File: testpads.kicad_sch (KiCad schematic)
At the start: 7 parts, among them J12 PinHeader_2x5_P1.27mm_SMD, J13 PinHeader_2x5_P1.27mm_SMD, J14 PinHeader_2x5_P1.27mm_SMD, J15 PinHeader_2x5_P1.27mm_SMD, J16 PinHeader_2x5_P1.27mm_SMD, J17 PinHeader_2x5_P1.27mm_SMD, J20 PinHeader_2x5_P1.27mm_SMD

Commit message: [#93514] Propagate title and date across all of the sheets
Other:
- title: (none) -> Datacenter Secure Control Module Breakout Board
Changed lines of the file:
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@@
 	(generator_version "9.0")
 	(paper "A3")
+	(title_block
+		(title "Datacenter Secure Control Module Breakout Board")
+		(date "2021-12-16")
+		(rev "2.0.0")
+	)
 	(text "I2C"
 		(exclude_from_sim no)

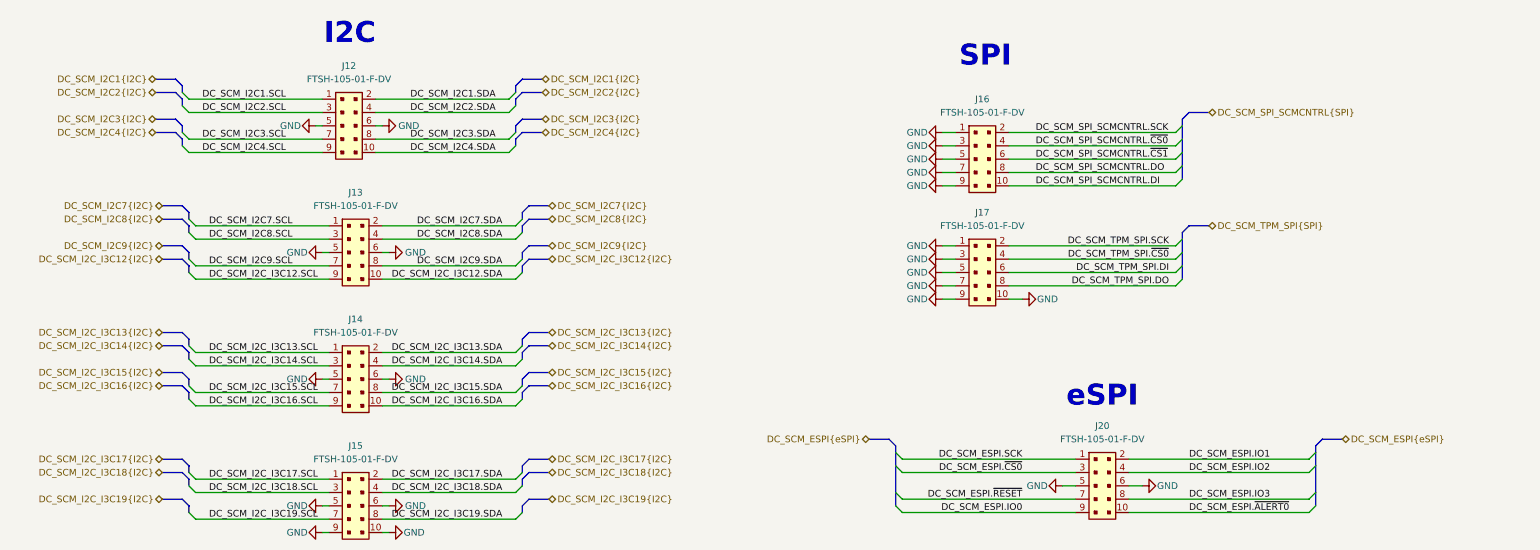
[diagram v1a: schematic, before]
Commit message: [#93514] Move SPI to one header
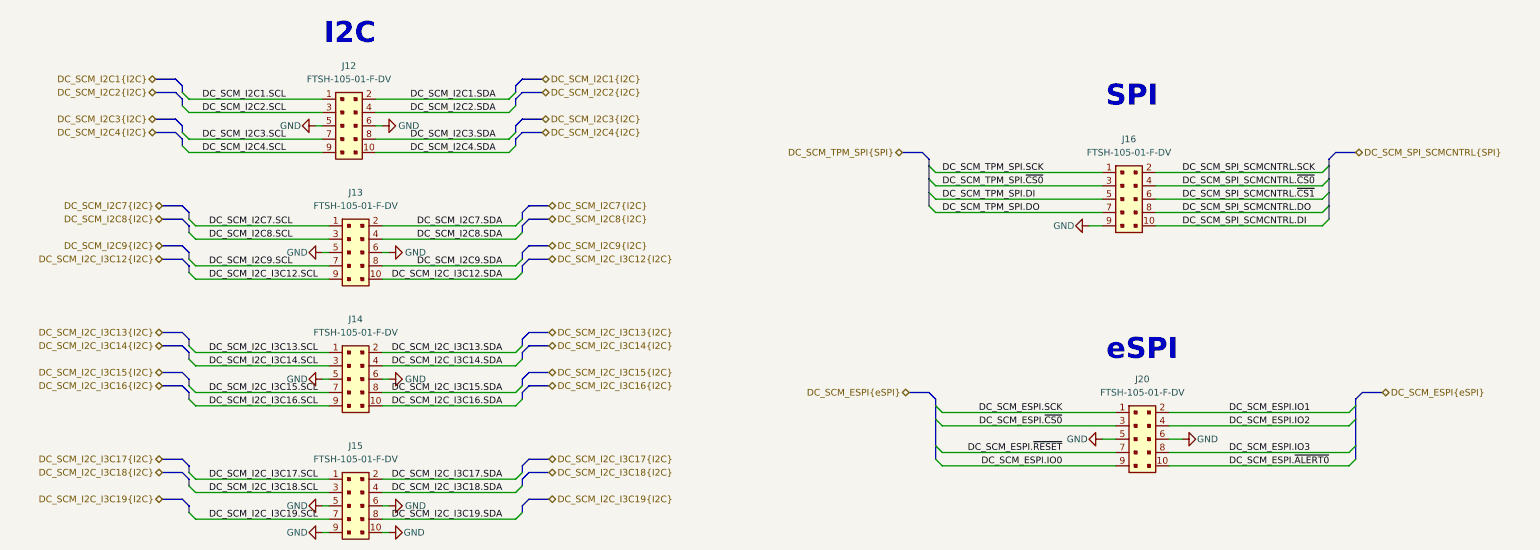
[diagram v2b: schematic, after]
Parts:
- removed J17: PinHeader_2x5_P1.27mm_SMD, antmicro-footprints:PinHeader_2x5_P1.27mm_SMD, symbol antmicroGenericPinHeaders:PinHeader_2x5_P1.27mm_SMD
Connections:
- net DC_SCM_TPM_SPI.DI: now also J16.5
- net DC_SCM_TPM_SPI.DO: now also J16.7
- net DC_SCM_TPM_SPI.SCK: now also J16.1
- net DC_SCM_TPM_SPI.~{CS0}: now also J16.3
- net GND: no longer J16.1, J16.3, J16.5, J16.7
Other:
- moved on the sheet: J16, J20
